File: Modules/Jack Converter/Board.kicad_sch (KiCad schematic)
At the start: 32 parts, among them J1 TS_Jack_3.5mm_Sw, J10 TS_Jack_6.35mm_Sw, J100 IDC_02x08, J11 TS_Jack_3.5mm_Sw, J12 TS_Jack_6.35mm_Sw, J13 TS_Jack_3.5mm_Sw, J14 TS_Jack_6.35mm_Sw, J15 TS_Jack_3.5mm_Sw, J16 TS_Jack_6.35mm_Sw, J17 TS_Jack_3.5mm_Sw, J18 TS_Jack_6.35mm_Sw, J19 TS_Jack_3.5mm_Sw, J2 TS_Jack_6.35mm_Sw, J20 TS_Jack_6.35mm_Sw, J3 TS_Jack_3.5mm_Sw, J4 TS_Jack_6.35mm_Sw, J5 TS_Jack_3.5mm_Sw, J50 Conn_01x08_BackboneTap, J6 TS_Jack_6.35mm_Sw, J7 TS_Jack_3.5mm_Sw, J8 TS_Jack_6.35mm_Sw, J9 TS_Jack_3.5mm_Sw, SW1 SW_DPDT, SW2 SW_DPDT, SW3 SW_DPDT

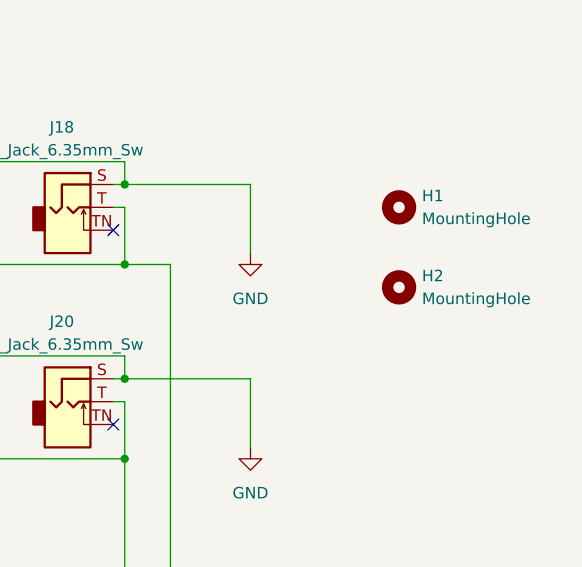
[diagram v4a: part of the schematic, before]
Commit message: Sent banana jack and switch pinheaders to the back
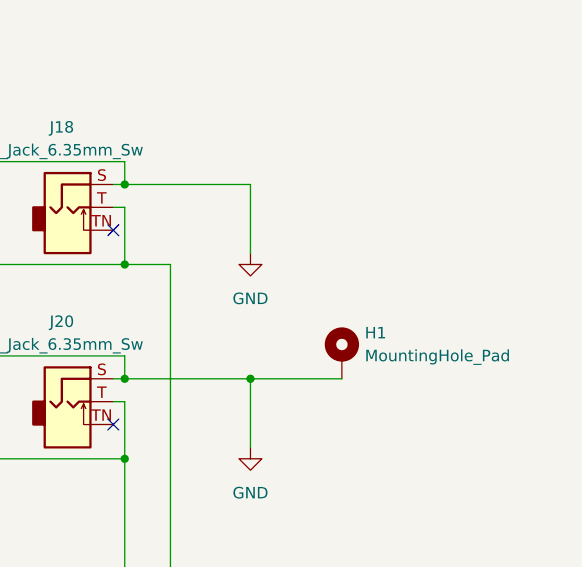
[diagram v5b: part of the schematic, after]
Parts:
- removed H1: MountingHole, MountingHole:MountingHole_3.2mm_M3, symbol Mechanical:MountingHole
- H1: renamed from H2; value MountingHole -> MountingHole_Pad; footprint MountingHole:MountingHole_3.2mm_M3 -> SynthStuff:MountingHole_3.2mm_M3_Pad4mm; symbol Mechanical:MountingHole -> Mechanical:MountingHole_Pad
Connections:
- net GND: now also H1.1
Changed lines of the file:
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@@
 	)
 	(junction
+		(at 219.71 60.96)
+		(diameter 0)
+		(color 0 0 0 0)
+	)
+	(junction
 		(at 160.02 109.22)
 		(diameter 0)
@@
 	(wire
 		(pts
+			(xy 219.71 60.96) (xy 229.87 60.96)
+		)
+		(stroke
+			(width 0)
+			(type default)
+		)
+	)
+	(wire
+		(pts
 			(xy 160.02 107.95) (xy 160.02 109.22)
 		)
@@
 	)
 	(symbol
-		(lib_id "Mechanical:MountingHole")
-		(at 236.22 50.8 0)
+		(lib_id "Mechanical:MountingHole_Pad")
+		(at 229.87 58.42 0)
 		(unit 1)
 		(exclude_from_sim yes)
@@
 		(dnp no)
 		(fields_autoplaced yes)
-		(property "Reference" "H2"
-			(at 238.76 49.5299 0)
+		(property "Reference" "H1"
+			(at 232.41 55.8799 0)
 			(effects
 				(font
@@
 			)
 		)
-		(property "Value" "MountingHole"
-			(at 238.76 52.0699 0)
+		(property "Value" "MountingHole_Pad"
+			(at 232.41 58.4199 0)
 			(effects
 				(font
@@
 			)
 		)
-		(property "Footprint" "MountingHole:MountingHole_3.2mm_M3"
-			(at 236.22 50.8 0)
+		(property "Footprint" "SynthStuff:MountingHole_3.2mm_M3_Pad4mm"
+			(at 229.87 58.42 0)
 			(effects
 				(font
@@
 		)
 		(property "Datasheet" "~"
-			(at 236.22 50.8 0)
+			(at 229.87 58.42 0)
 			(effects
 				(font
@@
 			)
 		)
-		(property "Description" "Mounting Hole without connection"
-			(at 236.22 50.8 0)
+		(property "Description" "Mounting Hole with connection"
+			(at 229.87 58.42 0)
 			(effects
 				(font
@@
 			)
 		)
+		(pin "1"
+		)
 		(instances
 			(project "Jack Converter"
 				(path "/b497d75e-0918-4e9c-ae43-36360bc031dc/01b3bf80-fded-40b5-ad81-2678b7ef607a"
-					(reference "H2")
+					(reference "H1")
 					(unit 1)
 				)
@@
 					(unit 1)
 				)
-			)
-		)
-	)
-	(symbol
-		(lib_id "Mechanical:MountingHole")
-		(at 236.22 41.91 0)
-		(unit 1)
-		(exclude_from_sim yes)
-		(in_bom no)
-		(on_board yes)
-		(dnp no)
-		(fields_autoplaced yes)
-		(property "Reference" "H1"
-			(at 238.76 40.6399 0)
-			(effects
-				(font
-					(size 1.27 1.27)
-				)
-				(justify left)
-			)
-		)
-		(property "Value" "MountingHole"
-			(at 238.76 43.1799 0)
-			(effects
-				(font
-					(size 1.27 1.27)
-				)
-				(justify left)
-			)
-		)
-		(property "Footprint" "MountingHole:MountingHole_3.2mm_M3"
-			(at 236.22 41.91 0)
-			(effects
-				(font
-					(size 1.27 1.27)
-				)
-				(hide yes)
-			)
-		)
-		(property "Datasheet" "~"
-			(at 236.22 41.91 0)
-			(effects
-				(font
-					(size 1.27 1.27)
-				)
-				(hide yes)
-			)
-		)
-		(property "Description" "Mounting Hole without connection"
-			(at 236.22 41.91 0)
-			(effects
-				(font
-					(size 1.27 1.27)
-				)
-				(hide yes)
-			)
-		)
-		(instances
-			(project "Jack Converter"
-				(path "/b497d75e-0918-4e9c-ae43-36360bc031dc/01b3bf80-fded-40b5-ad81-2678b7ef607a"
-					(reference "H1")
-					(unit 1)
-				)

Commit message: Removed spacer hole and updated sheets
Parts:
- removed H1: MountingHole_Pad, SynthStuff:MountingHole_3.2mm_M3_Pad4mm, symbol Mechanical:MountingHole_Pad
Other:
- company: (none) -> DMH
- title: (none) -> Adapter Mult Mk1
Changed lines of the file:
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@@
 	(generator_version "8.0")
 	(paper "A4")
+	(title_block
+		(title "Adapter Mult Mk1")
+		(date "2024-05-26")
+		(rev "1")
+		(company "DMH")
+	)
 	(junction
 		(at 100.33 167.64)
@@
 	)
 	(junction
-		(at 219.71 60.96)
-		(diameter 0)
-		(color 0 0 0 0)
-	)
-	(junction
 		(at 160.02 109.22)
 		(diameter 0)
@@
 	(wire
 		(pts
-			(xy 219.71 60.96) (xy 229.87 60.96)
-		)
-		(stroke
-			(width 0)
-			(type default)
-		)
-	)
-	(wire
-		(pts
 			(xy 160.02 107.95) (xy 160.02 109.22)
 		)
@@
 					(unit 1)
 				)
-			)
-		)
-	)
-	(symbol
-		(lib_id "Mechanical:MountingHole_Pad")
-		(at 229.87 58.42 0)
-		(unit 1)
-		(exclude_from_sim yes)
-		(in_bom no)
-		(on_board yes)
-		(dnp no)
-		(fields_autoplaced yes)
-		(property "Reference" "H1"
-			(at 232.41 55.8799 0)
-			(effects
-				(font
-					(size 1.27 1.27)
-				)
-				(justify left)
-			)
-		)
-		(property "Value" "MountingHole_Pad"
-			(at 232.41 58.4199 0)
-			(effects
-				(font
-					(size 1.27 1.27)
-				)
-				(justify left)
-			)
-		)
-		(property "Footprint" "SynthStuff:MountingHole_3.2mm_M3_Pad4mm"
-			(at 229.87 58.42 0)
-			(effects
-				(font
-					(size 1.27 1.27)
-				)
-				(hide yes)
-			)
-		)
-		(property "Datasheet" "~"
-			(at 229.87 58.42 0)
-			(effects
-				(font
-					(size 1.27 1.27)
-				)
-				(hide yes)
-			)
-		)
-		(property "Description" "Mounting Hole with connection"
-			(at 229.87 58.42 0)
-			(effects
-				(font
-					(size 1.27 1.27)
-				)
-				(hide yes)
-			)
-		)
-		(pin "1"
-		)
-		(instances
-			(project "Jack Converter"
-				(path "/b497d75e-0918-4e9c-ae43-36360bc031dc/01b3bf80-fded-40b5-ad81-2678b7ef607a"
-					(reference "H1")
-					(unit 1)
-				)
